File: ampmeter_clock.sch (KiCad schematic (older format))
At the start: 115 parts, among them J1 Barrel_Jack, Q1 2N7000, Q10 2N7000, Q11 2N7000, Q12 2N7000, Q13 2N7000, Q14 2N7000, Q15 2N7000, Q16 2N7000, Q17 2N7000, Q18 2N7000, Q19 2N7000, Q2 2N7000, Q20 IRF5305PBF, Q3 2N7000, Q4 2N7000, Q5 2N7000, Q6 2N7000, Q7 2N7000, Q8 2N7000, Q9 2N7000, SW1 SET_MIN, SW2 SET_HOUR, SW3 RESET, U1 4027, U10 4516, U11 4516, U2 40106, U3 40106, U4 4081, U5 4081, U6 4060, U7 4510, U8 4516, U9 4510, Y1 32.768kHz

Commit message: Fix bugs
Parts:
- removed R16, R24, R29: 4k7, symbol Device:R_Small
- added D2, D3, D4, D5, D6, D7: 1N4148, Diode_THT:D_DO-35_SOD27_P7.62mm_Horizontal, symbol Diode:1N4148
- added R16, R24: 4k7, symbol Device:R
- added R29: 4K7, symbol Device:R
- added SW4: CLK_HALT, symbol Switch:SW_Push
- C12, C13: value 33pF -> 22pF
- R4: value 330k -> 470k
- R8: value 6M8 -> 4k7
- R9: value 6M8 -> 10M
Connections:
- net +5V: now also SW1.3, SW2.3, SW3.3, R16.1, R24.1, SW4.1
- net CLK: now also U1.13 (C), U10.15 (CLK), U11.15 (CLK), U9.15 (CLK); no longer SW1.1, SW2.1
- net GND: now also R8.2, U1.11 (K), U3.3, U3.9, R29.2; no longer U11.1 (PE), U4.12, U4.13, U6.12 (RST)
- net HOUR_3: now also U4.12; no longer U5.12
- net RST: now also D7.2 (A); no longer U1.12 (R)
- net RST_STAGE3: now also U11.1 (PE), D6.2 (A); no longer U1.11 (K)
- net ~CO_STAGE1: now also D3.1 (K); no longer U9.5 (CI)
- net ~CO_STAGE2: now also D5.1 (K); no longer U11.5 (CI)
- net at U11.7 (CO), U2.11: now also U4.13
- net at R4.1, U6.10 (OSCRES): now also R9.1; no longer R8.1
- net at U4.11: now also U5.12
- net at U3.2: now also D2.1 (K); no longer U3.3
- net at U3.6: now also D4.1 (K); no longer U3.9
- removed net CLK_STAGE2: U10.15 (CLK), U3.4, U9.15 (CLK)
- removed net CLK_STAGE3: U1.13 (C), U11.15 (CLK), U3.8
- new net: D6.1 (K), D7.1 (K), R29.1, U1.12 (R)
- new net: R8.1, SW4.2, U6.12 (RST)
- new net ~CI_STAGE2: D2.2 (A), D3.2 (A), R16.2, U9.5 (CI)
- new net ~CI_STAGE3: D4.2 (A), D5.2 (A), R24.2, U11.5 (CI)
- no-connect marks 19 -> 22
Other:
- moved on the sheet: C1, C10, C11, C12, C13, C14, C15, C16, C17, C18, C2, C3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

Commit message: Component Placement
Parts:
- removed C18: 100uF, symbol Device:CP
- removed J1: Barrel_Jack, symbol Connector:Barrel_Jack
- removed Q1, Q10, Q11, Q12, Q13, Q14, Q15, Q16, Q17, Q18, Q19, Q2, Q3, Q4, Q5, Q6, Q7, Q8, Q9: 2N7000, Package_TO_SOT_THT:TO-92_Inline, symbol Transistor_FET:2N7000
- removed Q20: IRF5305PBF, symbol Device:Q_PMOS_GDS
- removed SW1: SET_MIN, symbol Switch:SW_SPDT_MSM
- removed SW2: SET_HOUR, symbol Switch:SW_SPDT_MSM
- removed SW3: RESET, symbol Switch:SW_SPDT_MSM
- added D10, D11, D12, D13, D14, D15, D16, D17, D18, D19, D20, D21, D22, D23, D24, D25, D26, D27, D8, D9: LED, LED_SMD:LED_0603_1608Metric, symbol Device:LED
- added J1: Barrel_Jack_Switch, Connector_BarrelJack:BarrelJack_Horizontal, symbol Connector:Barrel_Jack_Switch
- added Q1, Q10, Q11, Q12, Q13, Q14, Q15, Q16, Q17, Q18, Q19, Q2, Q3, Q4, Q5, Q6, Q7, Q8, Q9: 2N7002, Package_TO_SOT_SMD:SOT-23, symbol Transistor_FET:2N7002
- added Q20: NCE30P12S, Package_SO:SOIC-8_3.9x4.9mm_P1.27mm, symbol ampmeter_clock:NCE30P12S
- added RN1, RN2, RN3, RN4, RN5, RN6: 4k7, Resistor_SMD:R_Array_Convex_4x0603, symbol Device:R_Pack04
- added SW1: SET_MIN, TS-1101:TS-1101, symbol Switch:SW_Push
- added SW2: SET_HOUR, TS-1101:TS-1101, symbol Switch:SW_Push
- added SW3: RESET, TS-1101:TS-1101, symbol Switch:SW_Push
- C1, C10, C11, C12, C13, C14, C15, C16, C2, C3, C4, C5, C6, C7, C8, C9: footprint (none) -> Capacitor_SMD:C_0603_1608Metric
- C17: value 100uF -> 470uF; footprint (none) -> Capacitor_THT:CP_Radial_D8.0mm_P3.50mm
- D1: value BZX55C6V2 -> ZMM6V2; footprint (none) -> Diode_SMD:D_MiniMELF
- D2, D3, D4, D5, D6, D7: footprint Diode_THT:D_DO-35_SOD27_P7.62mm_Horizontal -> Diode_SMD:D_MiniMELF
- MES1, MES2, MES3: footprint (none) -> TerminalBlock:TerminalBlock_bornier-2_P5.08mm
- R1, R10, R11, R12, R13, R14, R15, R16, R17, R18, R19, R2, R20, R21, R22, R23, R24, R25, R26, R27, R28, R29, R3, R30, R31, R32, R33, R34, R35, R36, R37, R38, R4, R5, R6, R7, R8: footprint (none) -> Resistor_SMD:R_0603_1608Metric
- R9: footprint (none) -> Resistor_SMD:R_0805_2012Metric
- RV1, RV10, RV11, RV12, RV13, RV14, RV15, RV16, RV17, RV18, RV19, RV2, RV3, RV4, RV5, RV6, RV7, RV8, RV9: footprint (none) -> 3362P:3362P_1
- SW4: footprint (none) -> TS-1101:TS-1101
- U1, U10, U11, U6, U7, U8, U9: footprint (none) -> Package_DIP:DIP-16_W7.62mm
- U2, U3, U4, U5: footprint (none) -> Package_DIP:DIP-14_W7.62mm
- Y1: footprint (none) -> Crystal:Crystal_Round_D2.0mm_Vertical
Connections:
- net +5V: now also Q20.1 (S), Q20.2 (S), Q20.3 (S), SW1.1, SW2.1, SW3.1
- net CLK: now also D13.2 (A)
- net GND: now also J1.2, Q1.2 (S), Q10.2 (S), Q11.2 (S), Q12.2 (S), Q13.2 (S), Q14.2 (S), Q15.2 (S), Q16.2 (S), Q17.2 (S), Q18.2 (S), Q19.2 (S), Q2.2 (S), Q3.2 (S), Q4.2 (S), Q5.2 (S), Q6.2 (S), Q7.2 (S), Q8.2 (S), Q9.2 (S), RN1.5 (R4.2), RN1.6 (R3.2), RN1.7 (R2.2), RN1.8 (R1.2), RN2.5 (R4.2), RN2.6 (R3.2), RN2.7 (R2.2), RN2.8 (R1.2), RN3.5 (R4.2), RN3.6 (R3.2), RN3.7 (R2.2), RN3.8 (R1.2), RN4.5 (R4.2), RN4.6 (R3.2), RN4.7 (R2.2), RN4.8 (R1.2), RN5.5 (R4.2), RN5.6 (R3.2), RN5.7 (R2.2), RN5.8 (R1.2), RN6.5 (R4.2), RN6.6 (R3.2), RN6.7 (R2.2), RN6.8 (R1.2)
- net HOUR_0: now also D8.2 (A)
- net HOUR_1: now also D9.2 (A)
- net HOUR_2: now also D10.2 (A)
- net HOUR_3: now also D11.2 (A)
- net HOUR_4: now also D12.2 (A)
- net MIN_0: now also D14.2 (A)
- net MIN_1: now also D15.2 (A)
- net MIN_2: now also D16.2 (A)
- net MIN_3: now also D17.2 (A)
- net MIN_4: now also D18.2 (A)
- net MIN_5: now also D19.2 (A)
- net MIN_6: now also D20.2 (A)
- net SEC_0: now also D21.2 (A)
- net SEC_1: now also D22.2 (A)
- net SEC_2: now also D23.2 (A)
- net SEC_3: now also D24.2 (A)
- net SEC_4: now also D25.2 (A)
- net SEC_5: now also D26.2 (A)
- net SEC_6: now also D27.2 (A)
- net at C14.1, R20.1, U3.1: now also SW1.2
- net at C15.1, R25.1, U3.5: now also SW2.2
- net at C16.1, R30.1, U3.13: now also SW3.2
- net at R7.1: now also Q3.1 (G)
- net at RV3.1, RV3.2: now also R3.1
- net at R3.2: now also Q3.3 (D); no longer RV3.3
- net at MES3.1 (-), RV12.3, RV15.3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: now also RV3.3, RV6.3, RV9.3; no longer R12.1, R19.1, R3.1
- net at R15.1: now also Q6.1 (G)
- net at RV6.1, RV6.2: now also R12.1
- net at R12.2: now also Q6.3 (D); no longer RV6.3
- net at R23.1: now also Q9.1 (G)
- net at RV9.1, RV9.2: now also R19.1
- net at R19.2: now also Q9.3 (D); no longer RV9.3
- net at R28.1: now also Q12.1 (G)
- net at RV12.1, RV12.2: now also Q12.3 (D)
- net at R33.1: now also Q15.1 (G)
- net at RV15.1, RV15.2: now also Q15.3 (D)
- net at R35.1: now also Q17.1 (G)
- net at RV17.1, RV17.2: now also Q17.3 (D)
- net at R37.1: now also Q19.1 (G)
- net at RV19.1, RV19.2: now also Q19.3 (D)
- net at R6.1: now also Q2.1 (G)
- net at RV2.1, RV2.2: now also R2.1
- net at R2.2: now also Q2.3 (D); no longer RV2.3
- net at MES2.1 (-), RV11.3, RV14.3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: now also RV2.3, RV5.3, RV8.3; no longer R11.1, R18.1, R2.1
- net at R14.1: now also Q5.1 (G)
- net at RV5.1, RV5.2: now also R11.1
- net at R11.2: now also Q5.3 (D); no longer RV5.3
- net at R22.1: now also Q8.1 (G)
- net at RV8.1, RV8.2: now also R18.1
- net at R18.2: now also Q8.3 (D); no longer RV8.3
- net at R27.1: now also Q11.1 (G)
- net at RV11.1, RV11.2: now also Q11.3 (D)
- net at R32.1: now also Q14.1 (G)
- net at RV14.1, RV14.2: now also Q14.3 (D)
- net at R34.1: now also Q16.1 (G)
- net at RV16.1, RV16.2: now also Q16.3 (D)
- net at R36.1: now also Q18.1 (G)
- net at RV18.1, RV18.2: now also Q18.3 (D)
- net at R5.1: now also Q1.1 (G)
- net at RV1.1, RV1.2: now also R1.1
- net at R1.2: now also Q1.3 (D); no longer RV1.3
- net at MES1.1 (-), RV10.3, RV13.3: now also RV1.3, RV4.3, RV7.3; no longer R1.1, R10.1, R17.1
- net at R13.1: now also Q4.1 (G)
- net at RV4.1, RV4.2: now also R10.1
- net at R10.2: now also Q4.3 (D); no longer RV4.3
- net at R21.1: now also Q7.1 (G)
- net at RV7.1, RV7.2: now also R17.1
- net at R17.2: now also Q7.3 (D); no longer RV7.3
- net at R26.1: now also Q10.1 (G)
- net at RV10.1, RV10.2: now also Q10.3 (D)
- net at R31.1: now also Q13.1 (G)
- net at RV13.1, RV13.2: now also Q13.3 (D)
- net at R38.1: now also Q20.4 (G)
- new net: J1.1, Q20.5 (D), Q20.6 (D), Q20.7 (D), Q20.8 (D)
- new net: D8.1 (K), RN1.1 (R1.1)
- new net: D9.1 (K), RN1.2 (R2.1)
- new net: D10.1 (K), RN1.3 (R3.1)
- new net: D11.1 (K), RN1.4 (R4.1)
- new net: D12.1 (K), RN2.1 (R1.1)
- new net: D13.1 (K), RN2.4 (R4.1)
- new net: D14.1 (K), RN3.1 (R1.1)
- new net: D15.1 (K), RN3.2 (R2.1)
- new net: D16.1 (K), RN3.3 (R3.1)
- new net: D17.1 (K), RN3.4 (R4.1)
- new net: D18.1 (K), RN4.1 (R1.1)
- new net: D19.1 (K), RN4.2 (R2.1)
- new net: D20.1 (K), RN4.3 (R3.1)
- new net: D21.1 (K), RN5.1 (R1.1)
- new net: D22.1 (K), RN5.2 (R2.1)
- new net: D23.1 (K), RN5.3 (R3.1)
- new net: D24.1 (K), RN5.4 (R4.1)
- new net: D25.1 (K), RN6.1 (R1.1)
- new net: D26.1 (K), RN6.2 (R2.1)
- new net: D27.1 (K), RN6.3 (R3.1)
- no-connect marks 22 -> 24
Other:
- note added: "Output Indicators"
- note added: "RE1CM471F12PT"
- moved on the sheet: C17, R1, R10, R11, R12, R17, R18, R19, R2, R3, RV1, RV2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

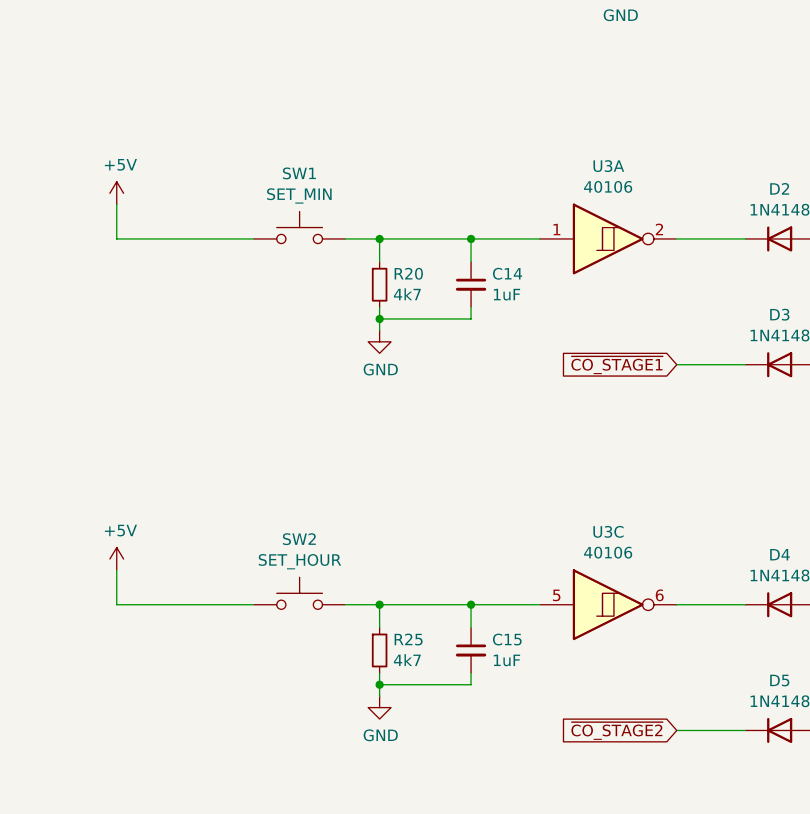
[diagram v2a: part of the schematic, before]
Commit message: Fix swapped H and M buttons and misc traces adjustments
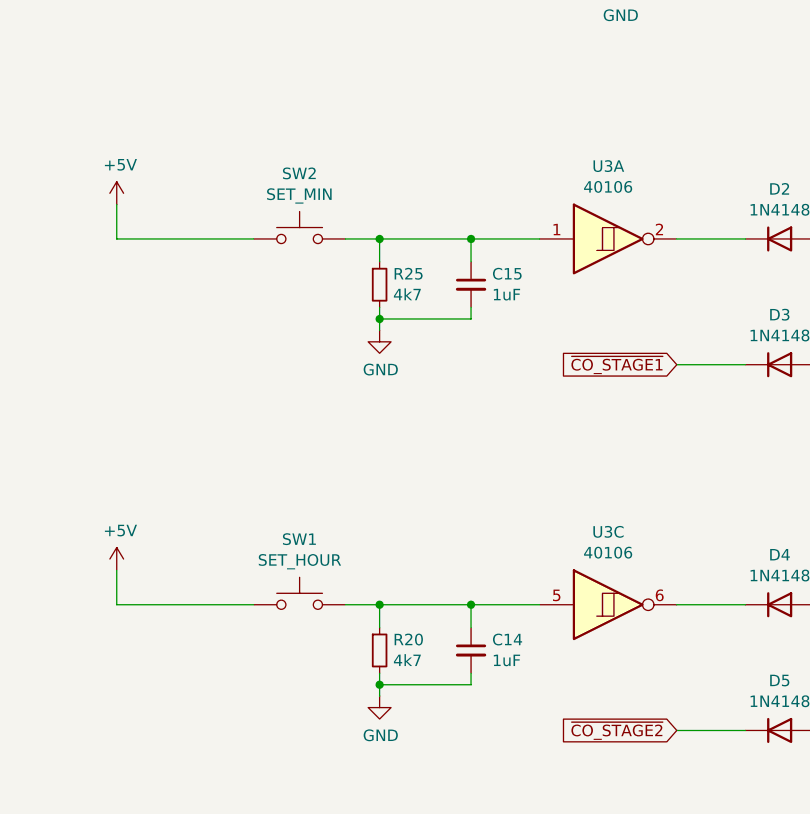
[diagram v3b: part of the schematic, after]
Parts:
- SW1: value SET_MIN -> SET_HOUR
- SW2: value SET_HOUR -> SET_MIN
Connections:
- net at C14.1, R20.1, SW1.2: now also U3.5; no longer U3.1
- net at C15.1, R25.1, SW2.2: now also U3.1; no longer U3.5
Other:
- moved on the sheet: C14, C15, R20, R25, SW1, SW2
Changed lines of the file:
@@
 	1    0    0    -1
 $EndComp
-$Comp
-L Device:R_Small R20
-U 1 1 61E12550
-P 2950 4600
-F 0 "R20" H 3009 4646 50  0000 L CNN
-F 1 "4k7" H 3009 4555 50  0000 L CNN
-F 2 "Resistor_SMD:R_0603_1608Metric" H 2950 4600 50  0001 C CNN
-F 3 "~" H 2950 4600 50  0001 C CNN
-	1    2950 4600
-	1    0    0    -1
-$EndComp
-$Comp
-L power:GND #PWR020
-U 1 1 61E12556
-P 2950 4800
-F 0 "#PWR020" H 2950 4550 50  0001 C CNN
-F 1 "GND" H 2955 4627 50  0000 C CNN
-F 2 "" H 2950 4800 50  0001 C CNN
-F 3 "" H 2950 4800 50  0001 C CNN
-	1    2950 4800
-	1    0    0    -1
-$EndComp
-Wire Wire Line
-	2800 4400 2950 4400
-Wire Wire Line
-	2950 4400 2950 4500
-Connection ~ 2950 4400
-Wire Wire Line
-	2950 4700 2950 4750
-$Comp
-L Device:R_Small R25
-U 1 1 61E24A80
-P 2950 6200
-F 0 "R25" H 3009 6246 50  0000 L CNN
-F 1 "4k7" H 3009 6155 50  0000 L CNN
-F 2 "Resistor_SMD:R_0603_1608Metric" H 2950 6200 50  0001 C CNN
-F 3 "~" H 2950 6200 50  0001 C CNN
-	1    2950 6200
-	1    0    0    -1
-$EndComp
-$Comp
-L power:GND #PWR026
-U 1 1 61E24A86
-P 2950 6400
-F 0 "#PWR026" H 2950 6150 50  0001 C CNN
-F 1 "GND" H 2955 6227 50  0000 C CNN
-F 2 "" H 2950 6400 50  0001 C CNN
-F 3 "" H 2950 6400 50  0001 C CNN
-	1    2950 6400
-	1    0    0    -1
-$EndComp
-Wire Wire Line
-	2800 6000 2950 6000
-Wire Wire Line
-	2950 6000 2950 6100
-Wire Wire Line
-	2950 6300 2950 6350
 Text GLabel 5350 7400 2    50   Output ~ 0
 RST
@@
 	1    0    0    -1
 $EndComp
-$Comp
-L Device:C_Small C14
-U 1 1 642DB7D6
-P 3350 4600
-F 0 "C14" H 3442 4646 50  0000 L CNN
-F 1 "1uF" H 3442 4555 50  0000 L CNN
-F 2 "Capacitor_SMD:C_0603_1608Metric" H 3350 4600 50  0001 C CNN
-F 3 "~" H 3350 4600 50  0001 C CNN
-	1    3350 4600
-	1    0    0    -1
-$EndComp
-Wire Wire Line
-	3350 4400 3350 4500
-Wire Wire Line
-	2950 4400 3350 4400
-Wire Wire Line
-	3350 4400 3650 4400
-Connection ~ 3350 4400
-Wire Wire Line
-	3350 4700 3350 4750
-Wire Wire Line
-	3350 4750 2950 4750
-Connection ~ 2950 4750
-Wire Wire Line
-	2950 4750 2950 4800
-$Comp
-L Device:C_Small C15
-U 1 1 643C0F17
-P 3350 6200
-F 0 "C15" H 3442 6246 50  0000 L CNN
-F 1 "1uF" H 3442 6155 50  0000 L CNN
-F 2 "Capacitor_SMD:C_0603_1608Metric" H 3350 6200 50  0001 C CNN
-F 3 "~" H 3350 6200 50  0001 C CNN
-	1    3350 6200
-	1    0    0    -1
-$EndComp
-Wire Wire Line
-	3350 6000 3350 6100
-Wire Wire Line
-	2950 6000 3350 6000
-Wire Wire Line
-	3350 6000 3650 6000
-Connection ~ 3350 6000
-Wire Wire Line
-	3350 6300 3350 6350
-Wire Wire Line
-	3350 6350 2950 6350
 Wire Wire Line
 	3350 7400 3350 7500
@@
 Wire Wire Line
 	4250 7400 4300 7400
-Connection ~ 2950 6000
-Connection ~ 2950 6350
-Wire Wire Line
-	2950 6350 2950 6400
 Connection ~ 2950 7400
 Connection ~ 2950 7750
@@
 $EndComp
 $Comp
-L Switch:SW_Push SW2
-U 1 1 61152B2C
-P 2600 6000
-F 0 "SW2" H 2600 6285 50  0000 C CNN
-F 1 "SET_HOUR" H 2600 6194 50  0000 C CNN
-F 2 "TS-1101:TS-1101" H 2600 6200 50  0001 C CNN
-F 3 "~" H 2600 6200 50  0001 C CNN
-	1    2600 6000
-	1    0    0    -1
-$EndComp
-$Comp
 L Switch:SW_Push SW3
 U 1 1 6115307E
@@
 	1800 4400 2400 4400
 $Comp
-L Switch:SW_Push SW1
-U 1 1 61150646
-P 2600 4400
-F 0 "SW1" H 2600 4685 50  0000 C CNN
-F 1 "SET_MIN" H 2600 4594 50  0000 C CNN
-F 2 "TS-1101:TS-1101" H 2600 4600 50  0001 C CNN
-F 3 "~" H 2600 4600 50  0001 C CNN
-	1    2600 4400
-	1    0    0    -1
-$EndComp
-$Comp
 L Device:LED D8
 U 1 1 612FA1DF
@@
 Text Notes 5100 14650 0    50   ~ 0
 RE1CM471F12PT
+$Comp
+L Device:R_Small R25
+U 1 1 61E24A80
+P 2950 4600
+F 0 "R25" H 3009 4646 50  0000 L CNN
+F 1 "4k7" H 3009 4555 50  0000 L CNN
+F 2 "Resistor_SMD:R_0603_1608Metric" H 2950 4600 50  0001 C CNN
+F 3 "~" H 2950 4600 50  0001 C CNN
+	1    2950 4600
+	1    0    0    -1
+$EndComp
+$Comp
+L power:GND #PWR026
+U 1 1 61E24A86
+P 2950 4800
+F 0 "#PWR026" H 2950 4550 50  0001 C CNN
+F 1 "GND" H 2955 4627 50  0000 C CNN
+F 2 "" H 2950 4800 50  0001 C CNN
+F 3 "" H 2950 4800 50  0001 C CNN
+	1    2950 4800
+	1    0    0    -1
+$EndComp
+Wire Wire Line
+	2800 4400 2950 4400
+Wire Wire Line
+	2950 4400 2950 4500
+Wire Wire Line
+	2950 4700 2950 4750
+$Comp
+L Device:C_Small C15
+U 1 1 643C0F17
+P 3350 4600
+F 0 "C15" H 3442 4646 50  0000 L CNN
+F 1 "1uF" H 3442 4555 50  0000 L CNN
+F 2 "Capacitor_SMD:C_0603_1608Metric" H 3350 4600 50  0001 C CNN
+F 3 "~" H 3350 4600 50  0001 C CNN
+	1    3350 4600
+	1    0    0    -1
+$EndComp
+Wire Wire Line
+	3350 4400 3350 4500
+Wire Wire Line
+	2950 4400 3350 4400
+Wire Wire Line
+	3350 4400 3650 4400
+Connection ~ 3350 4400
+Wire Wire Line
+	3350 4700 3350 4750
+Wire Wire Line
+	3350 4750 2950 4750
+Connection ~ 2950 4400
+Connection ~ 2950 4750
+Wire Wire Line
+	2950 4750 2950 4800
+$Comp
+L Switch:SW_Push SW2
+U 1 1 61152B2C
+P 2600 4400
+F 0 "SW2" H 2600 4685 50  0000 C CNN
+F 1 "SET_MIN" H 2600 4594 50  0000 C CNN
+F 2 "TS-1101:TS-1101" H 2600 4600 50  0001 C CNN
+F 3 "~" H 2600 4600 50  0001 C CNN
+	1    2600 4400
+	1    0    0    -1
+$EndComp
+$Comp
+L Device:R_Small R20
+U 1 1 61E12550
+P 2950 6200
+F 0 "R20" H 3009 6246 50  0000 L CNN
+F 1 "4k7" H 3009 6155 50  0000 L CNN
+F 2 "Resistor_SMD:R_0603_1608Metric" H 2950 6200 50  0001 C CNN
+F 3 "~" H 2950 6200 50  0001 C CNN
+	1    2950 6200
+	1    0    0    -1
+$EndComp
+$Comp
+L power:GND #PWR020
+U 1 1 61E12556
+P 2950 6400
+F 0 "#PWR020" H 2950 6150 50  0001 C CNN
+F 1 "GND" H 2955 6227 50  0000 C CNN
+F 2 "" H 2950 6400 50  0001 C CNN
+F 3 "" H 2950 6400 50  0001 C CNN
+	1    2950 6400
+	1    0    0    -1
+$EndComp
+Wire Wire Line
+	2800 6000 2950 6000
+Wire Wire Line
+	2950 6000 2950 6100
+Connection ~ 2950 6000
+Wire Wire Line
+	2950 6300 2950 6350
+$Comp
+L Device:C_Small C14
+U 1 1 642DB7D6
+P 3350 6200
+F 0 "C14" H 3442 6246 50  0000 L CNN
+F 1 "1uF" H 3442 6155 50  0000 L CNN
+F 2 "Capacitor_SMD:C_0603_1608Metric" H 3350 6200 50  0001 C CNN
+F 3 "~" H 3350 6200 50  0001 C CNN
+	1    3350 6200
+	1    0    0    -1
+$EndComp
+Wire Wire Line
+	3350 6000 3350 6100
+Wire Wire Line
+	2950 6000 3350 6000
+Wire Wire Line
+	3350 6000 3650 6000
+Connection ~ 3350 6000
+Wire Wire Line
+	3350 6300 3350 6350
+Wire Wire Line
+	3350 6350 2950 6350
+Connection ~ 2950 6350
+Wire Wire Line
+	2950 6350 2950 6400
+$Comp
+L Switch:SW_Push SW1
+U 1 1 61150646
+P 2600 6000
+F 0 "SW1" H 2600 6285 50  0000 C CNN
+F 1 "SET_HOUR" H 2600 6194 50  0000 C CNN
+F 2 "TS-1101:TS-1101" H 2600 6200 50  0001 C CNN
+F 3 "~" H 2600 6200 50  0001 C CNN
+	1    2600 6000
+	1    0    0    -1
+$EndComp
 $EndSCHEMATC
